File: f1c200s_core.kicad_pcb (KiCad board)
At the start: 2 copper layers, 22 x 30.3 mm, 66 parts, among them J1 NGFF_67P_M_KEY_Plug, SW1 FEL, SW2 FEL, U1 W25Q128JVS, U2 EA3036, U3 F1C200s, U4 XC6206PxxxMR, Y1 24MHz

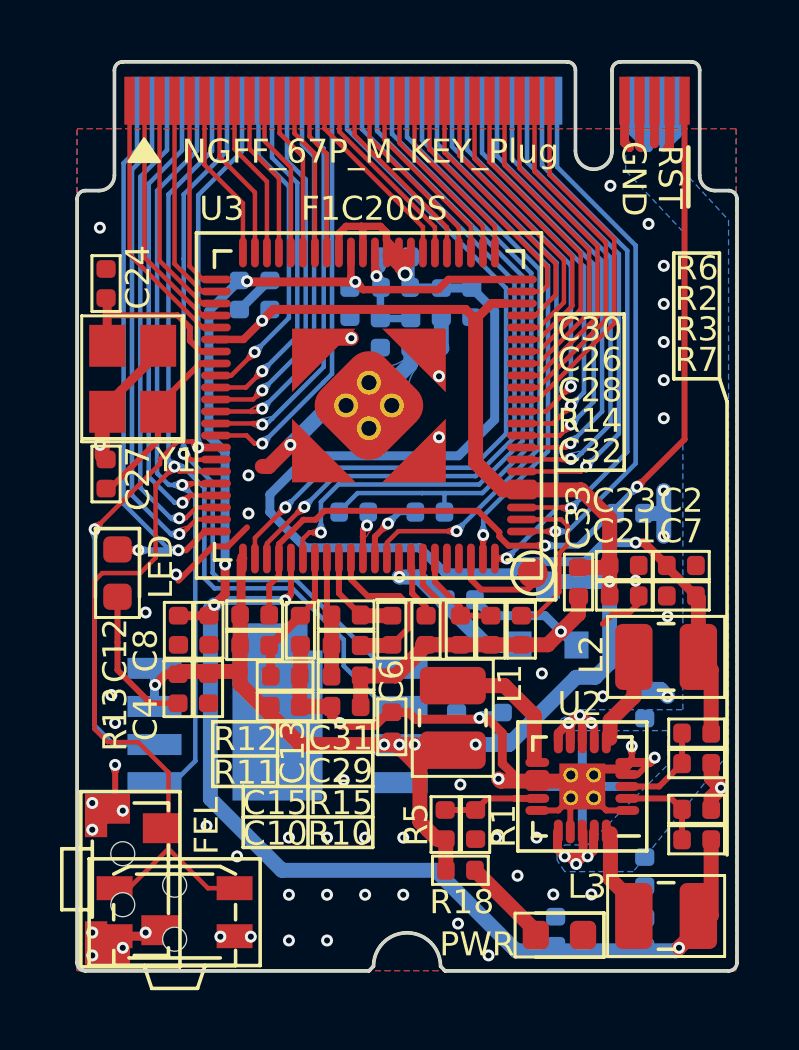
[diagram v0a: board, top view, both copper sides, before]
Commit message: Save as KiCad 6 project
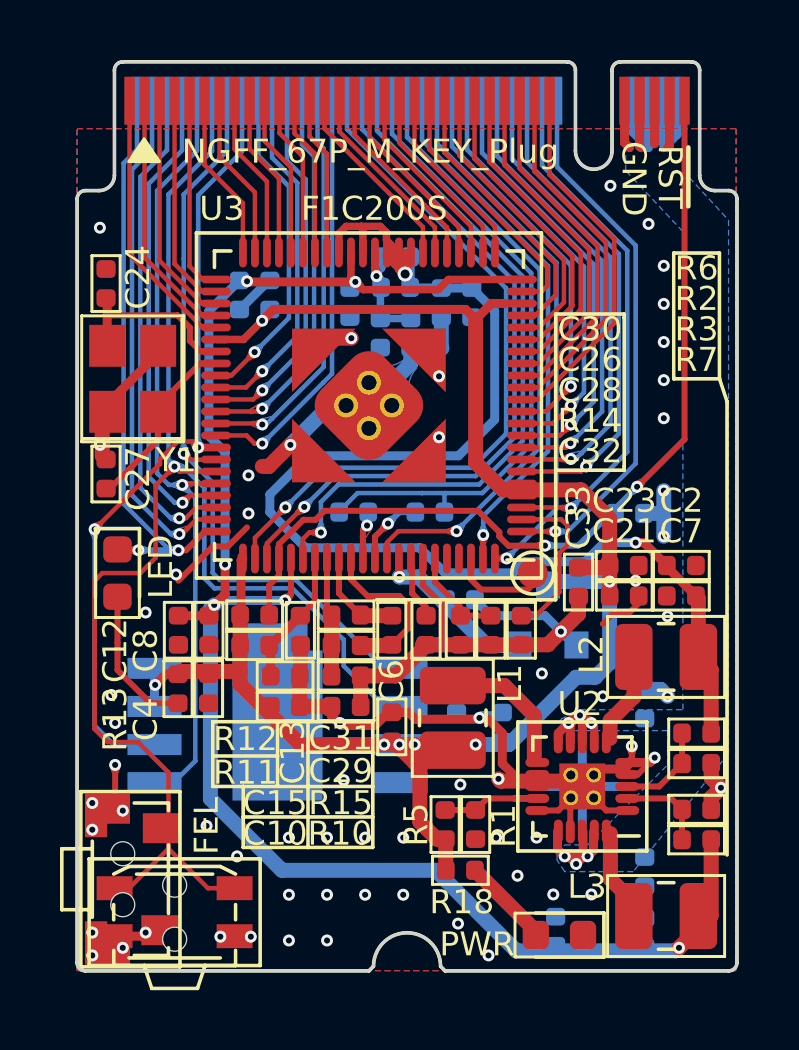
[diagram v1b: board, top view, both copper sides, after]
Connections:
- net /FLASH_~CS renamed /FLASH_~{CS}
- net /~RESET renamed /~{RESET}
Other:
- net class Default removed
- board text added: "~{RST}"
- board text removed: "~RST"
